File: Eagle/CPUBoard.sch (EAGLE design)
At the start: 19 parts, among them IC2 MAX232, IC3 MAX481CPA, X1 BUTTON_BOARD, X2 RELAY_BOARD, X3 RS-485, X4 DISPLAY, X5 RS-232, X6 MKDSN1,5/3-5,08, X7 MKDSN1,5/3-5,08

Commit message: - more stuff added
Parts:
- removed X1: BUTTON_BOARD, con-molex:KK-156-8
- added C10: 100n, rcl:C-EU025-025X050
- added C8, C9: 22p, resistor:C-EU025-024X044
- added Q1: (no value), special:XTAL/S
- added X8: BUTTON_BOARD, con-molex:KK-156-10
- X2: device con-molex:KK-156-9 -> con-molex:KK-156-8
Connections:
- new net +5V: C10.1, C3.-, C5.1, C6.1, IC1.AVCC, IC1.VCC, R1.2
- new net BUT_L: X8-6.S
- new net BUT_LL: X8-5.S
- new net BUT_R: X8-8.S
- new net BUT_RR: X8-9.S
- new net BUT_STOP: X8-7.S
- new net GND: C10.2, C4.+, C5.2, C6.2, C8.1, C9.1, IC1.GND@0, IC1.GND@1, JP1.3, JP1.4, JP1.6, JP1.8, X2-1.S, X8-10.S
- new net LED1: X8-1.S
- new net LED2: X8-2.S
- new net LED_L: X8-3.S
- new net LED_R: X8-4.S
- new net N$1: C9.2, IC1.XTAL1, Q1.2
- new net N$10: C4.-, IC2G$1.V-
- new net N$11: IC1.SCK/OC3B/PCINT15, JP1.7
- new net N$13: IC1.MISO/OC3A/PCINT14, JP1.9
- new net N$14: IC1.MOSI/ICP3/PCINT13, JP1.1
- new net N$2: C8.2, IC1.XTAL2, Q1.1
- new net N$3: IC1.RESET, JP1.5, R1.1
- new net N$5: C1.+, IC2G$1.C1+
- new net N$6: C1.-, IC2G$1.C1-
- new net N$7: C2.+, IC2G$1.C2+
- new net N$8: C2.-, IC2G$1.C2-
- new net N$9: C3.+, IC2G$1.V+
- new net SER1_CTS: IC2G$1.R2IN, X5-4.S
- new net SER1_RTS: IC2G$1.T2OUT, X5-5.S
- new net SER1_RXD: IC2G$1.R1IN, X5-3.S
- new net SER1_TXD: IC2G$1.T1OUT, X5-2.S
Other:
- moved on the sheet: C1, C2, C3, C4, C5, C6, IC1, IC2, JP1, R1, X2-1, X2-2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

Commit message: - CPUBoard near final ...
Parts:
- added L1: 10u, rcl:L-EU0207/10
- added R2, R3: 4k7, rcl:R-EU_0207/10
- added R4, R5: 470R, rcl:R-EU_0207/10
- added R6, R7: 680R, rcl:R-EU_0207/10
- IC3: value MAX481CPA -> MAX485CPA
- Q1: value (none) -> 12.000MHz
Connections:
- net N$11 renamed ENC_SCK
- net N$13 renamed ENC_SO
- net N$14 renamed ENC_SI
- removed net BUT_L: X8-6.S
- removed net BUT_LL: X8-5.S
- removed net BUT_R: X8-8.S
- removed net BUT_RR: X8-9.S
- removed net BUT_STOP: X8-7.S
- removed net LED1: X8-1.S
- removed net LED2: X8-2.S
- new net ENC_CS: IC1.SS/OC0B/PCINT12
- new net ENC_INT: IC1.AIN0/INT2/PCINT10
- new net LED_GREEN: R4.2, X8-1.S
- new net LED_YELLOW: R5.2, X8-2.S
- new net LEFT: IC1.ADC1/PCINT1, X8-6.S
- new net N$11: IC1.RXD1/INT0/PCINT26, IC2G$1.R1OUT
- new net N$12: C6.1, IC1.AVCC, L1.2
- new net N$13: IC1.T3/RXD0/PCINT24, IC3G$1.RO
- new net N$14: IC1.TXD0/PCINT25, IC3G$1.DI
- new net N$15: IC1.TOSC1/PCINT22, IC3G$1.DE, IC3G$1.RE/
- new net N$17: IC3G$1.A, X3-4.S
- new net N$18: IC3G$1.B, X3-2.S
- new net N$20: IC1.TCK/PCINT18, R4.1
- new net N$21: IC1.TMS/PCINT19, R5.1
- new net N$22: IC1.TDO/PCINT20, R6.1
- new net N$23: IC1.TDI/PCINT21, R7.1
- new net N$4: IC1.TXD1/INT1/PCINT27, IC2G$1.T1IN
- new net PRESET_LEFT: IC1.ADC3/PCINT3, X8-5.S
- new net PRESET_RIGHT: IC1.ADC4/PCINT4, X8-9.S
- new net REL1: IC1.OC2A/PCINT31, X2-2.S
- new net REL2: IC1.OC2B/ICP/PCINT30, X2-3.S
- new net REL3: IC1.OC1A/PCINT29, X2-4.S
- new net REL4: IC1.XCK1/OC1B/PCINT28, X2-5.S
- new net RIGHT: IC1.ADC2/PCINT2, X8-8.S
- new net SCL: IC1.SCL/PCINT16, R2.1, X4-1.S
- new net SDA: IC1.SDA/PCINT17, R3.1, X4-2.S
- new net SPARE: X4-3.S
- new net STOP: IC1.ADC0/PCINT0, X8-7.S
- net +5V: now also C7.1, L1.1, R2.2, R3.2, X3-1.S, X4-5.S, X6-1.KL, X7-1.KL; no longer C6.1, IC1.AVCC
- net GND: now also C7.2, X3-3.S, X3-5.S, X4-4.S, X5-1.S, X6-3.KL, X7-3.KL
- net LED_L: now also R6.2
- net LED_R: now also R7.2
- net SER1_CTS: now also IC2G$1.T2OUT; no longer IC2G$1.R2IN
- net SER1_RTS: now also IC2G$1.R2IN; no longer IC2G$1.T2OUT
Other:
- moved on the sheet: C1, C10, C2, C3, C4, C5, C6, C7, IC2, IC3, JP1, X5-1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

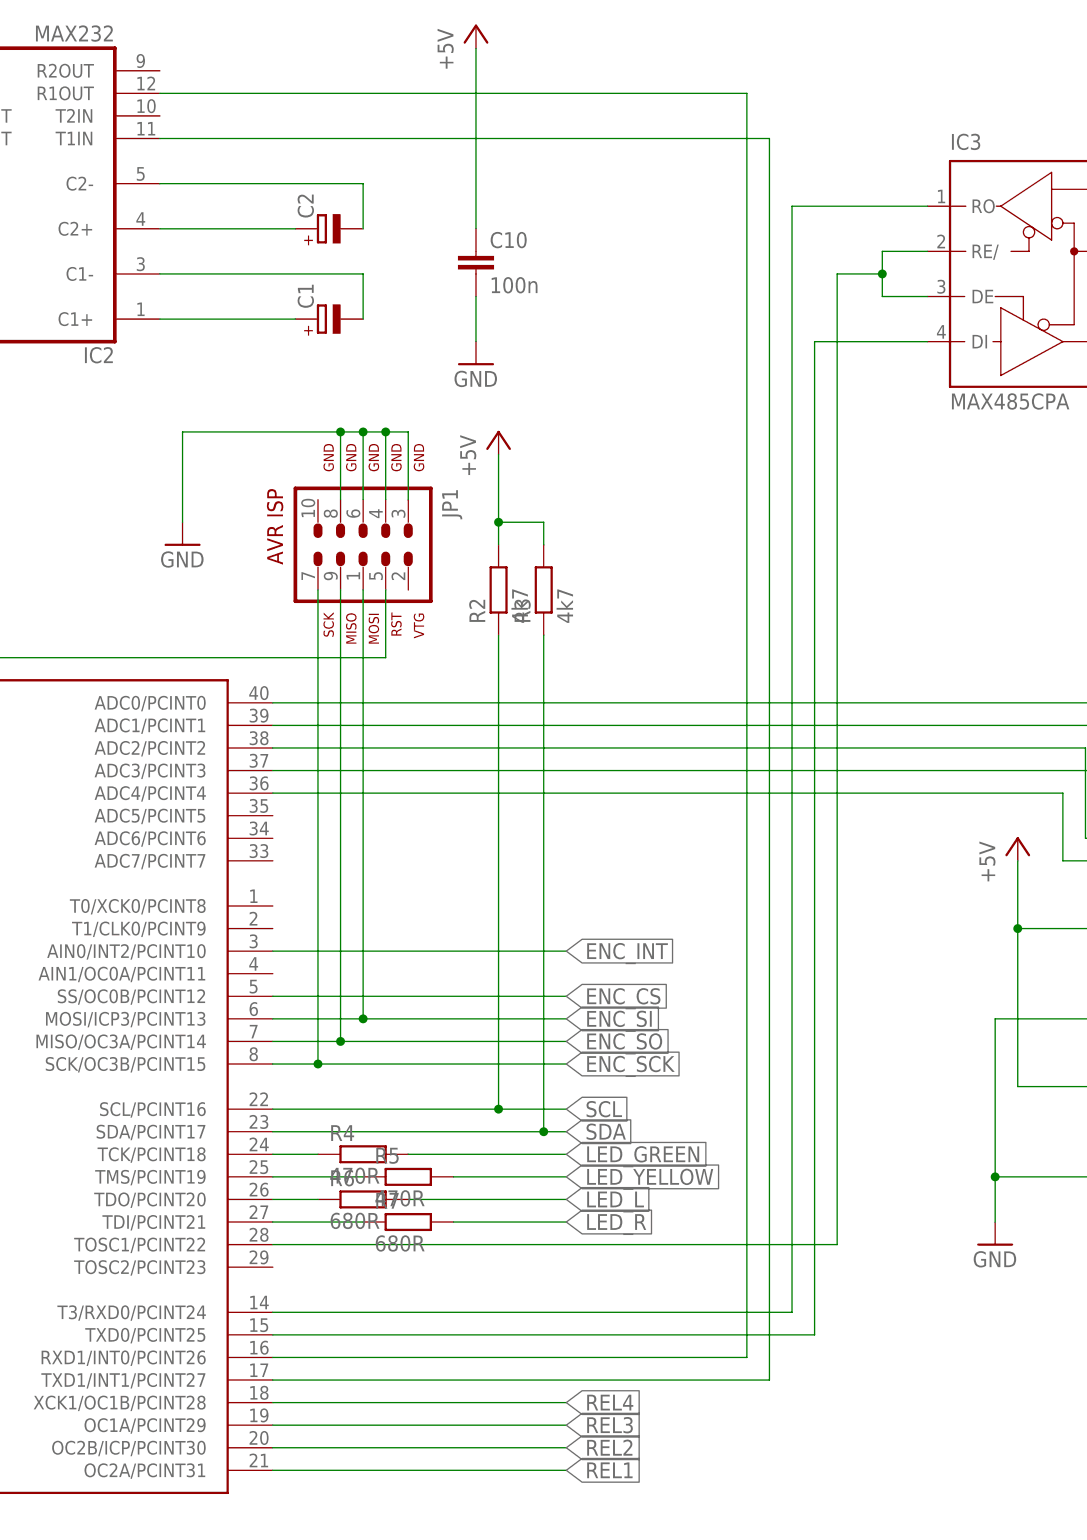
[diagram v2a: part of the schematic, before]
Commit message: - CPUBoard: jumper block for serial interface, MAX232 | USB
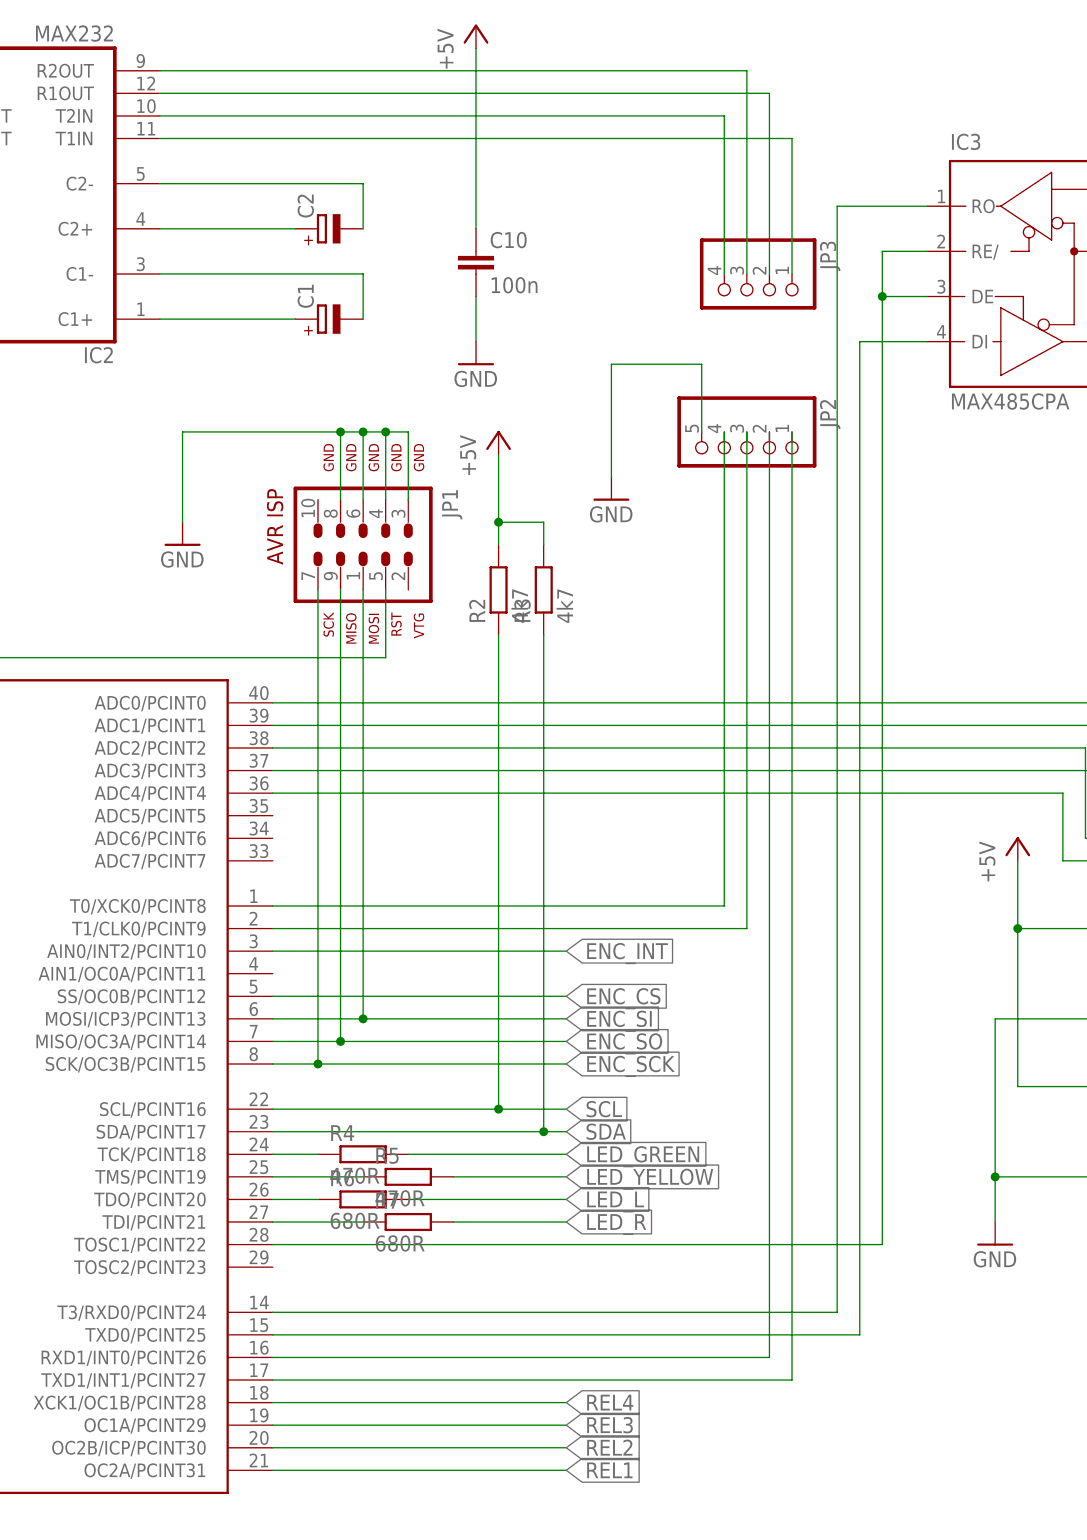
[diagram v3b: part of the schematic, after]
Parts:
- added JP2: (no value), pinhead:PINHD-1X5
- added JP3: (no value), pinhead:PINHD-1X4
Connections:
- new net N$16: IC1.RXD1/INT0/PCINT26, JP2.2
- new net N$24: IC1.TXD1/INT1/PCINT27, JP2.1
- new net N$28: IC2G$1.R2OUT, JP3.3
- new net N$29: IC2G$1.T2IN, JP3.4
- new net N$30: IC1.T1/CLK0/PCINT9, JP2.3
- new net N$31: IC1.T0/XCK0/PCINT8, JP2.4
- net GND: now also JP2.5
- net N$11: now also JP3.2; no longer IC1.RXD1/INT0/PCINT26
- net N$4: now also JP3.1; no longer IC1.TXD1/INT1/PCINT27
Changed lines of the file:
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@@
 <part name="R7" library="rcl" deviceset="R-EU_" device="0207/10" value="680R"/>
 <part name="GND8" library="supply1" deviceset="GND" device=""/>
+<part name="JP2" library="pinhead" deviceset="PINHD-1X5" device=""/>
+<part name="JP3" library="pinhead" deviceset="PINHD-1X4" device=""/>
+<part name="GND12" library="supply1" deviceset="GND" device=""/>
 </parts>
 <sheets>
@@
 <instance part="R7" gate="G$1" x="106.68" y="43.18"/>
 <instance part="GND8" gate="1" x="172.72" y="40.64"/>
+<instance part="JP2" gate="A" x="144.78" y="129.54" rot="R270"/>
+<instance part="JP3" gate="A" x="144.78" y="147.32" rot="R270"/>
+<instance part="GND12" gate="1" x="129.54" y="124.46"/>
 </instances>
 <busses>
@@
 <wire x1="172.72" y1="66.04" x2="185.42" y2="66.04" width="0.1524" layer="91"/>
 </segment>
+<segment>
+<pinref part="JP2" gate="A" pin="5"/>
+<wire x1="139.7" y1="132.08" x2="139.7" y2="139.7" width="0.1524" layer="91"/>
+<wire x1="139.7" y1="139.7" x2="129.54" y2="139.7" width="0.1524" layer="91"/>
+<pinref part="GND12" gate="1" pin="GND"/>
+<wire x1="129.54" y1="139.7" x2="129.54" y2="127" width="0.1524" layer="91"/>
+</segment>
 </net>
 <net name="N$1" class="0">
@@
 <net name="N$4" class="0">
 <segment>
-<pinref part="IC1" gate="G$1" pin="TXD1/INT1/PCINT27"/>
-<wire x1="91.44" y1="25.4" x2="147.32" y2="25.4" width="0.1524" layer="91"/>
-<wire x1="147.32" y1="25.4" x2="147.32" y2="165.1" width="0.1524" layer="91"/>
 <pinref part="IC2" gate="G$1" pin="T1IN"/>
-<wire x1="147.32" y1="165.1" x2="78.74" y2="165.1" width="0.1524" layer="91"/>
+<wire x1="149.86" y1="165.1" x2="78.74" y2="165.1" width="0.1524" layer="91"/>
+<pinref part="JP3" gate="A" pin="1"/>
+<wire x1="149.86" y1="149.86" x2="149.86" y2="165.1" width="0.1524" layer="91"/>
 </segment>
 </net>
@@
 <segment>
 <pinref part="IC2" gate="G$1" pin="R1OUT"/>
-<wire x1="78.74" y1="170.18" x2="144.78" y2="170.18" width="0.1524" layer="91"/>
-<wire x1="144.78" y1="170.18" x2="144.78" y2="27.94" width="0.1524" layer="91"/>
-<pinref part="IC1" gate="G$1" pin="RXD1/INT0/PCINT26"/>
-<wire x1="144.78" y1="27.94" x2="91.44" y2="27.94" width="0.1524" layer="91"/>
+<wire x1="78.74" y1="170.18" x2="147.32" y2="170.18" width="0.1524" layer="91"/>
+<pinref part="JP3" gate="A" pin="2"/>
+<wire x1="147.32" y1="149.86" x2="147.32" y2="170.18" width="0.1524" layer="91"/>
 </segment>
 </net>
@@
 <segment>
 <pinref part="IC3" gate="G$1" pin="RO"/>
-<wire x1="165.1" y1="157.48" x2="149.86" y2="157.48" width="0.1524" layer="91"/>
-<wire x1="149.86" y1="157.48" x2="149.86" y2="33.02" width="0.1524" layer="91"/>
+<wire x1="165.1" y1="157.48" x2="154.94" y2="157.48" width="0.1524" layer="91"/>
+<wire x1="154.94" y1="157.48" x2="154.94" y2="33.02" width="0.1524" layer="91"/>
 <pinref part="IC1" gate="G$1" pin="T3/RXD0/PCINT24"/>
-<wire x1="149.86" y1="33.02" x2="91.44" y2="33.02" width="0.1524" layer="91"/>
+<wire x1="154.94" y1="33.02" x2="91.44" y2="33.02" width="0.1524" layer="91"/>
 </segment>
 </net>
@@
 <segment>
 <pinref part="IC1" gate="G$1" pin="TXD0/PCINT25"/>
-<wire x1="91.44" y1="30.48" x2="152.4" y2="30.48" width="0.1524" layer="91"/>
-<wire x1="152.4" y1="30.48" x2="152.4" y2="142.24" width="0.1524" layer="91"/>
+<wire x1="91.44" y1="30.48" x2="157.48" y2="30.48" width="0.1524" layer="91"/>
+<wire x1="157.48" y1="30.48" x2="157.48" y2="142.24" width="0.1524" layer="91"/>
 <pinref part="IC3" gate="G$1" pin="DI"/>
-<wire x1="152.4" y1="142.24" x2="165.1" y2="142.24" width="0.1524" layer="91"/>
+<wire x1="157.48" y1="142.24" x2="165.1" y2="142.24" width="0.1524" layer="91"/>
 </segment>
 </net>
@@
 <pinref part="IC3" gate="G$1" pin="RE/"/>
 <wire x1="165.1" y1="152.4" x2="160.02" y2="152.4" width="0.1524" layer="91"/>
-<wire x1="160.02" y1="152.4" x2="160.02" y2="149.86" width="0.1524" layer="91"/>
 <pinref part="IC3" gate="G$1" pin="DE"/>
-<wire x1="160.02" y1="149.86" x2="160.02" y2="147.32" width="0.1524" layer="91"/>
 <wire x1="160.02" y1="147.32" x2="165.1" y2="147.32" width="0.1524" layer="91"/>
-<wire x1="160.02" y1="149.86" x2="154.94" y2="149.86" width="0.1524" layer="91"/>
-<junction x="160.02" y="149.86"/>
-<wire x1="154.94" y1="149.86" x2="154.94" y2="40.64" width="0.1524" layer="91"/>
+<wire x1="160.02" y1="152.4" x2="160.02" y2="147.32" width="0.1524" layer="91"/>
 <pinref part="IC1" gate="G$1" pin="TOSC1/PCINT22"/>
-<wire x1="154.94" y1="40.64" x2="91.44" y2="40.64" width="0.1524" layer="91"/>
+<wire x1="160.02" y1="147.32" x2="160.02" y2="40.64" width="0.1524" layer="91"/>
+<wire x1="160.02" y1="40.64" x2="91.44" y2="40.64" width="0.1524" layer="91"/>
+<junction x="160.02" y="147.32"/>
 </segment>
 </net>
@@
 </segment>
 </net>
+<net name="N$16" class="0">
+<segment>
+<pinref part="IC1" gate="G$1" pin="RXD1/INT0/PCINT26"/>
+<pinref part="JP2" gate="A" pin="2"/>
+<wire x1="147.32" y1="27.94" x2="91.44" y2="27.94" width="0.1524" layer="91"/>
+<wire x1="147.32" y1="132.08" x2="147.32" y2="27.94" width="0.1524" layer="91"/>
+</segment>
+</net>
+<net name="N$28" class="0">
+<segment>
+<pinref part="IC2" gate="G$1" pin="R2OUT"/>
+<wire x1="78.74" y1="172.72" x2="144.78" y2="172.72" width="0.1524" layer="91"/>
+<pinref part="JP3" gate="A" pin="3"/>
+<wire x1="144.78" y1="172.72" x2="144.78" y2="149.86" width="0.1524" layer="91"/>
+</segment>
+</net>
+<net name="N$29" class="0">
+<segment>
+<pinref part="JP3" gate="A" pin="4"/>
+<wire x1="142.24" y1="149.86" x2="142.24" y2="167.64" width="0.1524" layer="91"/>
+<pinref part="IC2" gate="G$1" pin="T2IN"/>
+<wire x1="142.24" y1="167.64" x2="78.74" y2="167.64" width="0.1524" layer="91"/>
+</segment>
+</net>
+<net name="N$30" class="0">
+<segment>
+<pinref part="JP2" gate="A" pin="3"/>
+<wire x1="144.78" y1="132.08" x2="144.78" y2="76.2" width="0.1524" layer="91"/>
+<pinref part="IC1" gate="G$1" pin="T1/CLK0/PCINT9"/>
+<wire x1="144.78" y1="76.2" x2="91.44" y2="76.2" width="0.1524" layer="91"/>
+</segment>
+</net>
+<net name="N$31" class="0">
+<segment>
+<pinref part="IC1" gate="G$1" pin="T0/XCK0/PCINT8"/>
+<wire x1="91.44" y1="78.74" x2="142.24" y2="78.74" width="0.1524" layer="91"/>
+<pinref part="JP2" gate="A" pin="4"/>
+<wire x1="142.24" y1="78.74" x2="142.24" y2="132.08" width="0.1524" layer="91"/>
+</segment>
+</net>
+<net name="N$24" class="0">
+<segment>
+<pinref part="JP2" gate="A" pin="1"/>
+<wire x1="149.86" y1="132.08" x2="149.86" y2="25.4" width="0.1524" layer="91"/>
+<pinref part="IC1" gate="G$1" pin="TXD1/INT1/PCINT27"/>
+<wire x1="91.44" y1="25.4" x2="149.86" y2="25.4" width="0.1524" layer="91"/>
+</segment>
+</net>
